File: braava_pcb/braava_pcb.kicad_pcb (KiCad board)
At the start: 2 copper layers, 6 parts, among them J1 Conn_01x18, J2 Conn_01x18

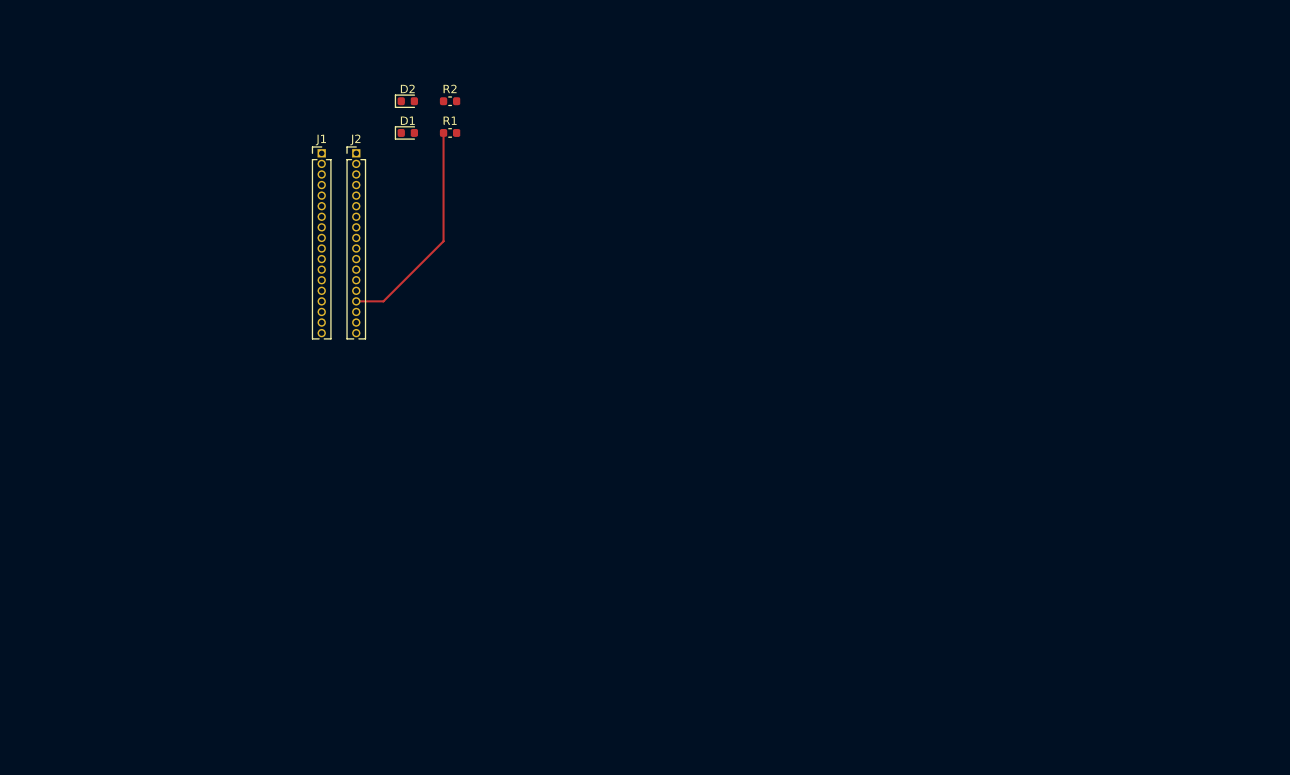
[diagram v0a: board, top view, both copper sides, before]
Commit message: Added touch switches library. Started component placement.
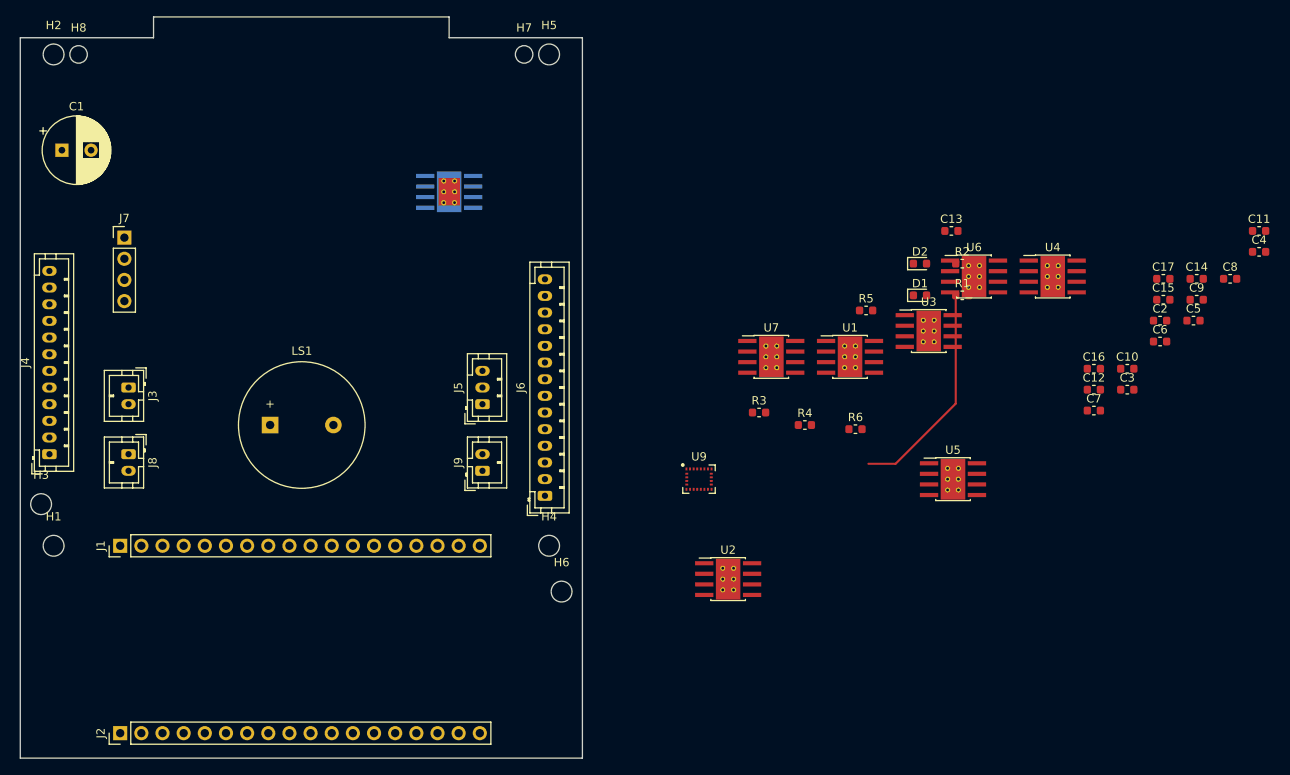
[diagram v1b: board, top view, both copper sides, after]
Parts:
- added C1: CP, Capacitor_THT:CP_Radial_D8.0mm_P3.50mm, F.Cu at (105.0, 77.0)
- added C10: 100nF, Capacitor_SMD:C_0603_1608Metric, F.Cu at (232.9, 103.2)
- added C11: 47uF, Capacitor_SMD:C_0603_1608Metric, F.Cu at (248.8, 86.7)
- added C12: 0.1uF, Capacitor_SMD:C_0603_1608Metric, F.Cu at (228.9, 105.8)
- added C13: 47uF, Capacitor_SMD:C_0603_1608Metric, F.Cu at (211.8, 86.7)
- added C14: 0.1uF, Capacitor_SMD:C_0603_1608Metric, F.Cu at (241.3, 92.4)
- added C15: 100nF, Capacitor_SMD:C_0603_1608Metric, F.Cu at (237.3, 95.0)
- added C16: 100nF, Capacitor_SMD:C_0603_1608Metric, F.Cu at (228.9, 103.2)
- added C17: 10uF, Capacitor_SMD:C_0603_1608Metric, F.Cu at (237.3, 92.4)
- added C2: 1uF, Capacitor_SMD:C_0603_1608Metric, F.Cu at (236.9, 97.5)
- added C3: 1uF, Capacitor_SMD:C_0603_1608Metric, F.Cu at (232.9, 105.8)
- added C4: 1uF, Capacitor_SMD:C_0603_1608Metric, F.Cu at (248.8, 89.2)
- added C5: 47uF, Capacitor_SMD:C_0603_1608Metric, F.Cu at (240.9, 97.5)
- added C6: 0.1uF, Capacitor_SMD:C_0603_1608Metric, F.Cu at (236.9, 100.0)
- added C7: 47uF, Capacitor_SMD:C_0603_1608Metric, F.Cu at (228.9, 108.3)
- added C8: 0.1uF, Capacitor_SMD:C_0603_1608Metric, F.Cu at (245.3, 92.4)
- added C9: 10nF(16V), Capacitor_SMD:C_0603_1608Metric, F.Cu at (241.3, 95.0)
- added H1: MountingHole, MountingHole:MountingHole_2.5mm, F.Cu at (104.0, 124.5)
- added H2: MountingHole, MountingHole:MountingHole_2.5mm, F.Cu at (104.0, 65.5)
- added H3: MountingHole, MountingHole:MountingHole_2.5mm, F.Cu at (102.5, 119.5)
- added H4: MountingHole, MountingHole:MountingHole_2.5mm, F.Cu at (163.5, 124.5)
- added H5: MountingHole, MountingHole:MountingHole_2.5mm, F.Cu at (163.5, 65.5)
- added H6: MountingHole, MountingHole:MountingHole_2.5mm, F.Cu at (165.0, 130.0)
- added H7: MountingHole, MountingHole:MountingHole_2.1mm, F.Cu at (160.5, 65.5)
- added H8: MountingHole, MountingHole:MountingHole_2.1mm, F.Cu at (107.0, 65.5)
- added J3: Conn_01x02, Connector_JST:JST_PH_B2B-PH-K_1x02_P2.00mm_Vertical, F.Cu at (113.0, 105.5)
- added J4: Conn_01x12, Connector_JST:JST_PH_B12B-PH-K_1x12_P2.00mm_Vertical, F.Cu at (103.5, 113.5)
- added J5: BAT_Conn_01x03, Connector_JST:JST_PH_B3B-PH-K_1x03_P2.00mm_Vertical, F.Cu at (155.5, 107.5)
- added J6: Conn_01x14, Connector_JST:JST_PH_B14B-PH-K_1x14_P2.00mm_Vertical, F.Cu at (163.0, 118.5)
- added J7: STEP_Conn_01x04, Connector_PinHeader_2.54mm:PinHeader_1x04_P2.54mm_Vertical, F.Cu at (112.5, 87.5)
- added J8: LMOT_Conn_01x02, Connector_JST:JST_PH_B2B-PH-K_1x02_P2.00mm_Vertical, F.Cu at (113.0, 113.5)
- added J9: RMOT_Conn_01x02, Connector_JST:JST_PH_B2B-PH-K_1x02_P2.00mm_Vertical, F.Cu at (155.5, 115.5)
- added LS1: Speaker, Buzzer_Beeper:Buzzer_15x7.5RM7.6, F.Cu at (130.0, 110.0)
- added R3: R, Resistor_SMD:R_0603_1608Metric, F.Cu at (188.7, 108.5)
- added R4: 4.7K, Resistor_SMD:R_0603_1608Metric, F.Cu at (194.2, 110.0)
- added R5: 4.7K, Resistor_SMD:R_0603_1608Metric, F.Cu at (201.6, 96.2)
- added R6: 4.7K, Resistor_SMD:R_0603_1608Metric, F.Cu at (200.3, 110.5)
- added U1: DRV8872DDA, Package_SO:Texas_HTSOP-8-1EP_3.9x4.9mm_P1.27mm_EP2.95x4.9mm_Mask2.4x3.1mm_ThermalVias, F.Cu at (199.6, 101.8)
- added U2: DRV8872DDA, Package_SO:Texas_HTSOP-8-1EP_3.9x4.9mm_P1.27mm_EP2.95x4.9mm_Mask2.4x3.1mm_ThermalVias, F.Cu at (185.0, 128.5)
- added U3: DRV8872DDA, Package_SO:Texas_HTSOP-8-1EP_3.9x4.9mm_P1.27mm_EP2.95x4.9mm_Mask2.4x3.1mm_ThermalVias, F.Cu at (209.1, 98.7)
- added U4: DRV8872DDA, Package_SO:Texas_HTSOP-8-1EP_3.9x4.9mm_P1.27mm_EP2.95x4.9mm_Mask2.4x3.1mm_ThermalVias, F.Cu at (224.0, 92.2)
- added U5: DRV8872DDA, Package_SO:Texas_HTSOP-8-1EP_3.9x4.9mm_P1.27mm_EP2.95x4.9mm_Mask2.4x3.1mm_ThermalVias, F.Cu at (212.0, 116.5)
- added U6: DRV8872DDA, Package_SO:Texas_HTSOP-8-1EP_3.9x4.9mm_P1.27mm_EP2.95x4.9mm_Mask2.4x3.1mm_ThermalVias, F.Cu at (214.5, 92.2)
- added U7: DRV8872DDA, Package_SO:Texas_HTSOP-8-1EP_3.9x4.9mm_P1.27mm_EP2.95x4.9mm_Mask2.4x3.1mm_ThermalVias, F.Cu at (190.2, 101.8)
- added U8: DRV8872DDA, Package_SO:Texas_HTSOP-8-1EP_3.9x4.9mm_P1.27mm_EP2.95x4.9mm_Mask2.4x3.1mm_ThermalVias, B.Cu at (151.5, 82.0)
- added U9: LSM9DS1, Package_LGA:LGA-24L_3x3.5mm_P0.43mm, F.Cu at (181.5, 116.5)
- J1, J2: footprint Connector_PinHeader_1.27mm:PinHeader_1x18_P1.27mm_Vertical -> Connector_PinHeader_2.54mm:PinHeader_1x18_P2.54mm_Vertical
- moved J2 75.2 mm to (112.0, 147.0), turned to 90 degrees
- moved D1 64.5 mm to (208.0, 94.4)
- moved D2 64.5 mm to (208.0, 90.6)
- moved R1 64.5 mm to (213.1, 94.4)
- moved R2 64.5 mm to (213.1, 90.6)
- moved J1 53.0 mm to (112.0, 124.5), turned to 90 degrees
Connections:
- J1 pad 1: Net-(J1-Pad1) -> /A0_PWM1
- J1 pad 10: Net-(J1-Pad10) -> /SW3_DRY
- J1 pad 11: Net-(J1-Pad11) -> /SDA
- J1 pad 12: Net-(J1-Pad12) -> /SCL
- J1 pad 13: Net-(J1-Pad13) -> /LDROP
- J1 pad 14: Net-(J1-Pad14) -> /LBUMP
- J1 pad 2: Net-(J1-Pad2) -> /A1_PWM2
- J1 pad 3: Net-(J1-Pad3) -> /RENCODER
- J1 pad 4: Net-(J1-Pad4) -> /LENCODER
- J1 pad 5: Net-(J1-Pad5) -> /SPEAKER
- J1 pad 8: Net-(J1-Pad8) -> /SW1_PWR
- J1 pad 9: Net-(J1-Pad9) -> /SW2_WET
- J2 pad 1: Net-(J2-Pad1) -> +3V3
- J2 pad 10: Net-(J2-Pad10) -> /RDROP
- J2 pad 11: Net-(J2-Pad11) -> /RBUMP
- J2 pad 12: Net-(J2-Pad12) -> /D6_PWM2
- J2 pad 13: Net-(J2-Pad13) -> /D5_PWM1
- J2 pad 17: Net-(J2-Pad17) -> /ESP_TX
- J2 pad 18: Net-(J2-Pad18) -> /ESP_RX
- J2 pad 4: Net-(J2-Pad4) -> GND
- J2 pad 5: Net-(J2-Pad5) -> /IO11_STEP1
- J2 pad 6: Net-(J2-Pad6) -> /IO8_STEP1
- J2 pad 7: Net-(J2-Pad7) -> /IO7_STEP1
- J2 pad 8: Net-(J2-Pad8) -> /IO6_STEP1
- J2 pad 9: Net-(J2-Pad9) -> /WEDGE
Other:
- board outline added: 67.5 x 89 mm
- copper layers 2 -> 4
